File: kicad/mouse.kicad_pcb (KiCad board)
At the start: 2 copper layers, 77 parts, among them IC1 L7805, P1 SOURCE_12v, P10 LED_CONN, P11 SW_CONN, P12 LED_K_CONN, P13 IR_SOURCE, P14 IR_CONN, P15 UI_SOURCE, P16 LED_K_CONN, P17 LED_CONN, P18 SW_CONN, P19 in12v -+ MOTOR_SOURCE, P2 SOURCE_12v, P20 in5v -+ CHIP_SOURCE, P21 MOTOR_CONTROL MOTOR_CONTROL, P22 MOTOR_L, P23 MOTOR_R, P3 battery 12v, P4 SOURCE_5v, P5 SOURCE_5v, P6 SOURCE_5v, P7 SOURCE_5v, P8 IR_CONN, P9 MOTOR_CONTROL, Q1 BSS138, Q2 BSS138, Q3 BSS138, Q4 BSS138, Q5 BSS138, Q6 BSS138, Q7 BSS138, SW1 SPST, SW2 SW_PUSH, SW3 SW_PUSH, SW4 SW_PUSH, U1 MCP3008, U2 LBR-127HLD, U3 LBR-127HLD, U4 LBR-127HLD, U5 LBR-127HLD

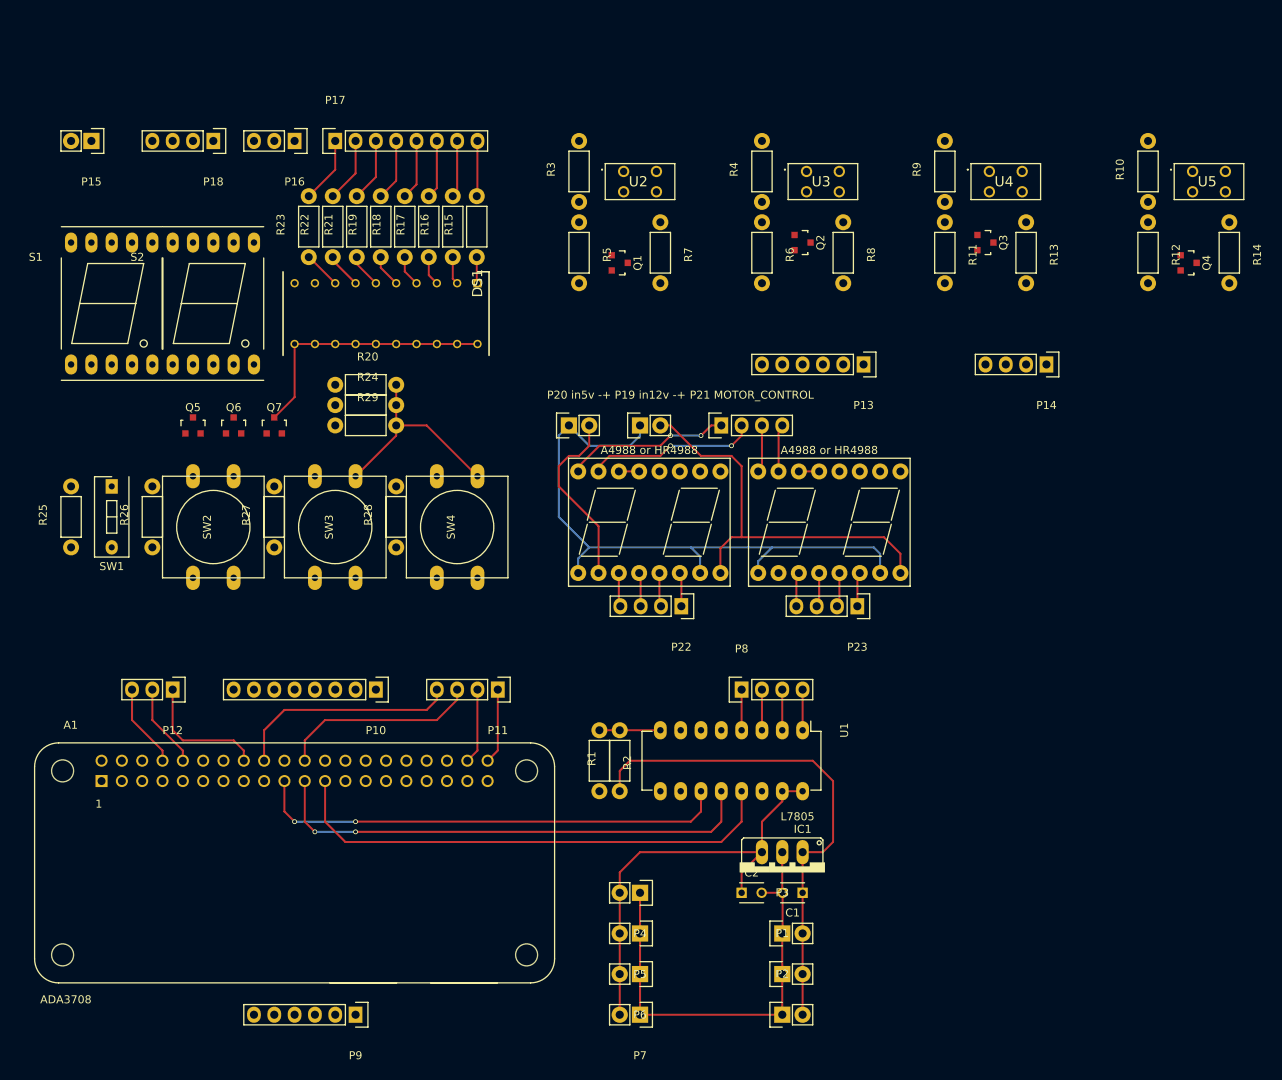
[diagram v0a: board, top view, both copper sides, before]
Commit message: add kicad
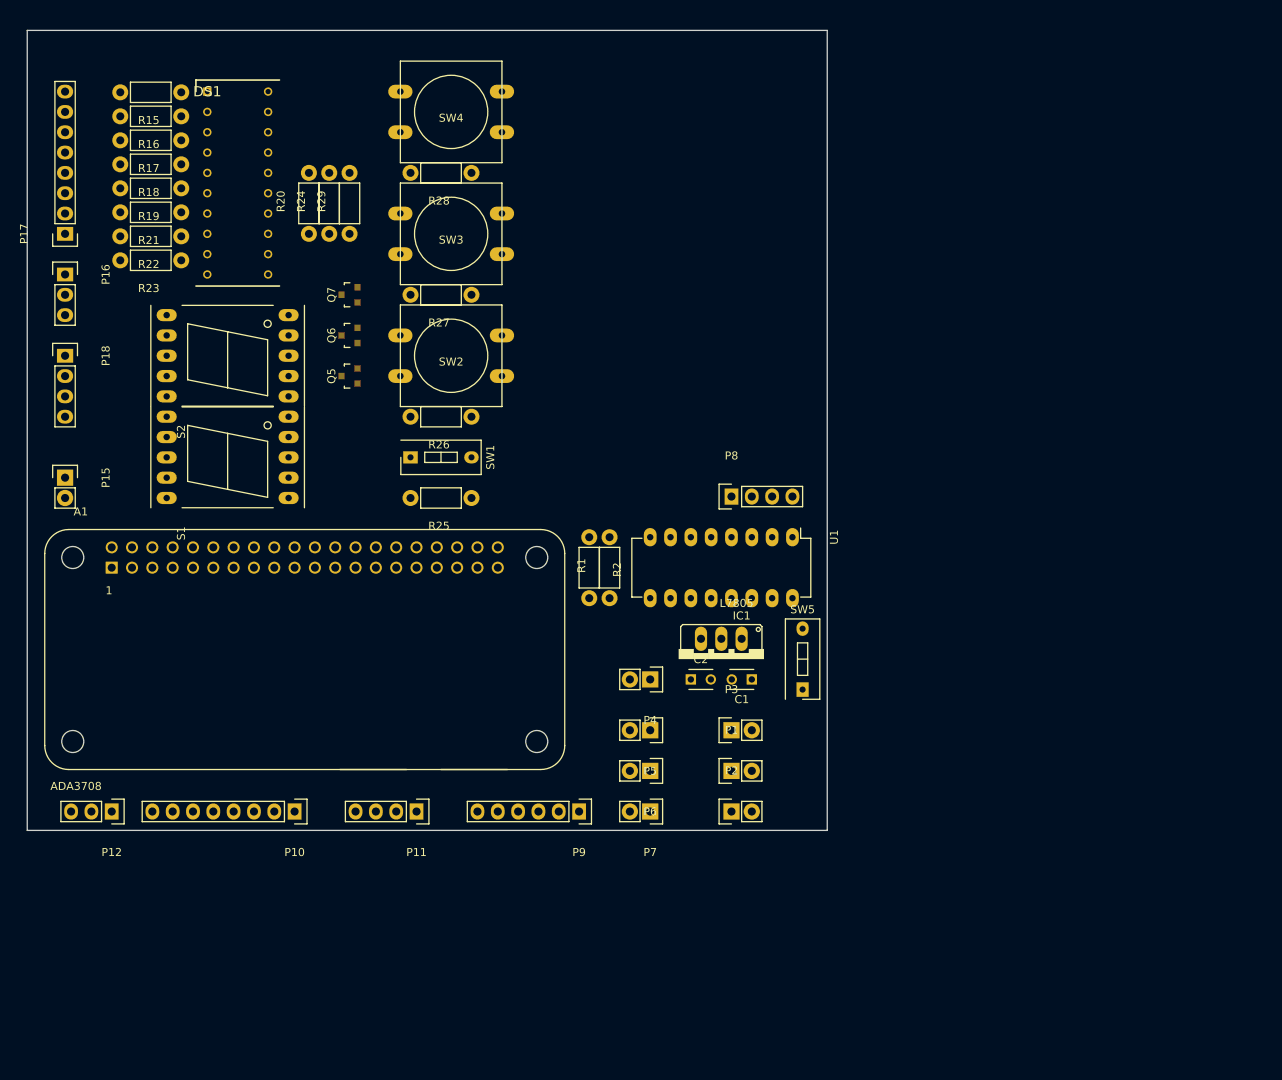
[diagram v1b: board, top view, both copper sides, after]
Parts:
- removed A4988 or HR4988: POLOLU_A4988, Displays_7-Segment:DA04 (x2)
- removed P13: IR_SOURCE, Socket_Strips:Socket_Strip_Straight_1x06
- removed P14: IR_CONN, Socket_Strips:Socket_Strip_Straight_1x04
- removed P19 in12v -+: MOTOR_SOURCE, Socket_Strips:Socket_Strip_Straight_1x02
- removed P20 in5v -+: CHIP_SOURCE, Socket_Strips:Socket_Strip_Straight_1x02
- removed P21 MOTOR_CONTROL: MOTOR_CONTROL, Socket_Strips:Socket_Strip_Straight_1x04
- removed P22: MOTOR_L, Socket_Strips:Socket_Strip_Straight_1x04
- removed P23: MOTOR_R, Socket_Strips:Socket_Strip_Straight_1x04
- removed Q1, Q2, Q3, Q4: BSS138, TO_SOT_Packages_SMD:SOT-23
- removed R10, R3, R4, R9: 10, Resistors_ThroughHole:Resistor_Horizontal_RM7mm
- removed R11, R12, R5, R6: 10k, Resistors_ThroughHole:Resistor_Horizontal_RM7mm
- removed R13, R14, R7, R8: 1k, Resistors_ThroughHole:Resistor_Horizontal_RM7mm
- removed U2, U3, U4, U5: LBR-127HLD, LBR-127HLD:A5131A
- added SW5: SPST, Buttons_Switches_ThroughHole:SW_DIP_x1_Slide, F.Cu at (121.9, 152.4)
- moved SW4 51.9 mm to (78.0, 80.2), turned to 180 degrees
- moved R25 50.4 mm to (80.5, 128.4), turned to 180 degrees
- moved R28 47.7 mm to (80.5, 87.8), turned to 180 degrees
- moved R26 43.1 mm to (80.5, 118.3), turned to 180 degrees
- moved R15 42.3 mm to (44.2, 77.7), turned to 180 degrees
- moved P15 42.2 mm to (29.7, 125.9), turned to 270 degrees
- moved DS1 41.4 mm to (47.5, 77.7), turned to 0 degrees
- moved R27 40.1 mm to (80.5, 103.0), turned to 180 degrees
- moved SW3 39.4 mm to (78.0, 95.4), turned to 180 degrees
- moved R16 38.2 mm to (44.2, 80.7), turned to 180 degrees
- moved P9 37.8 mm to (94.0, 167.6)
- moved SW1 37.5 mm to (72.9, 123.4), turned to 270 degrees
- moved SW2 36.6 mm to (78.0, 110.7), turned to 180 degrees
- moved P17 35.7 mm to (29.7, 95.4), turned to 90 degrees
- moved R17 34.2 mm to (44.2, 83.7), turned to 180 degrees
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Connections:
- P3 pad 2: Net-(C1-Pad1) -> Net-(P3-Pad2)
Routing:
- net Net-(P19-Pad1): track 79.6 -> 0.00 mm
- net Net-(C1-Pad1): track 63.1 -> 0.00 mm
- net Net-(A1-Pad23): track 63.1 -> 0.00 mm
- net Net-(A1-Pad21): track 62.0 -> 0.00 mm, vias 2 -> 0
- net Net-(A1-Pad19): track 59.5 -> 0.00 mm, vias 2 -> 0
- net GND: track 55.9 -> 0.00 mm
- net +5V: track 54.0 -> 0.00 mm
- net Net-(P19-Pad2): track 50.6 -> 0.00 mm
- net Net-(DS1-Pad11): track 33.1 -> 0.00 mm
- net SW1: track 28.2 -> 0.00 mm
- net Net-(P15-Pad1): track 26.3 -> 0.00 mm
- net SW2: track 25.0 -> 0.00 mm
- net Net-(P20-Pad2): track 22.8 -> 0.00 mm
- net Net-(P21-Pad2): track 21.9 -> 0.00 mm, vias 2 -> 0
- net Net-(P21-Pad1): track 21.2 -> 0.00 mm, vias 2 -> 0
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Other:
- board outline added: 100 x 100 mm

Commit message: add kicad
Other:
- board text added: "MechanicPlatypus MicroMouse"
- board text added: "made by powertimer811"
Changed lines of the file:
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@@
     (area 0 0 0 0)
     (thickness 1.6)
-    (drawings 6)
+    (drawings 8)
     (tracks 0)
     (zones 0)
@@
     )
   )
+  (gr_text "made by powertimer811" (at 120 90 90) (layer F.SilkS)
+    (effects (font (size 2 2) (thickness 0.3) italic))
+  )
+  (gr_text "MechanicPlatypus\nMicroMouse" (at 95 100 90) (layer F.SilkS)
+    (effects (font (size 4 4) (thickness 0.3) italic))
+  )
   (gr_line (start 125 70) (end 25 70) (angle 90) (layer Edge.Cuts) (width 0.15))

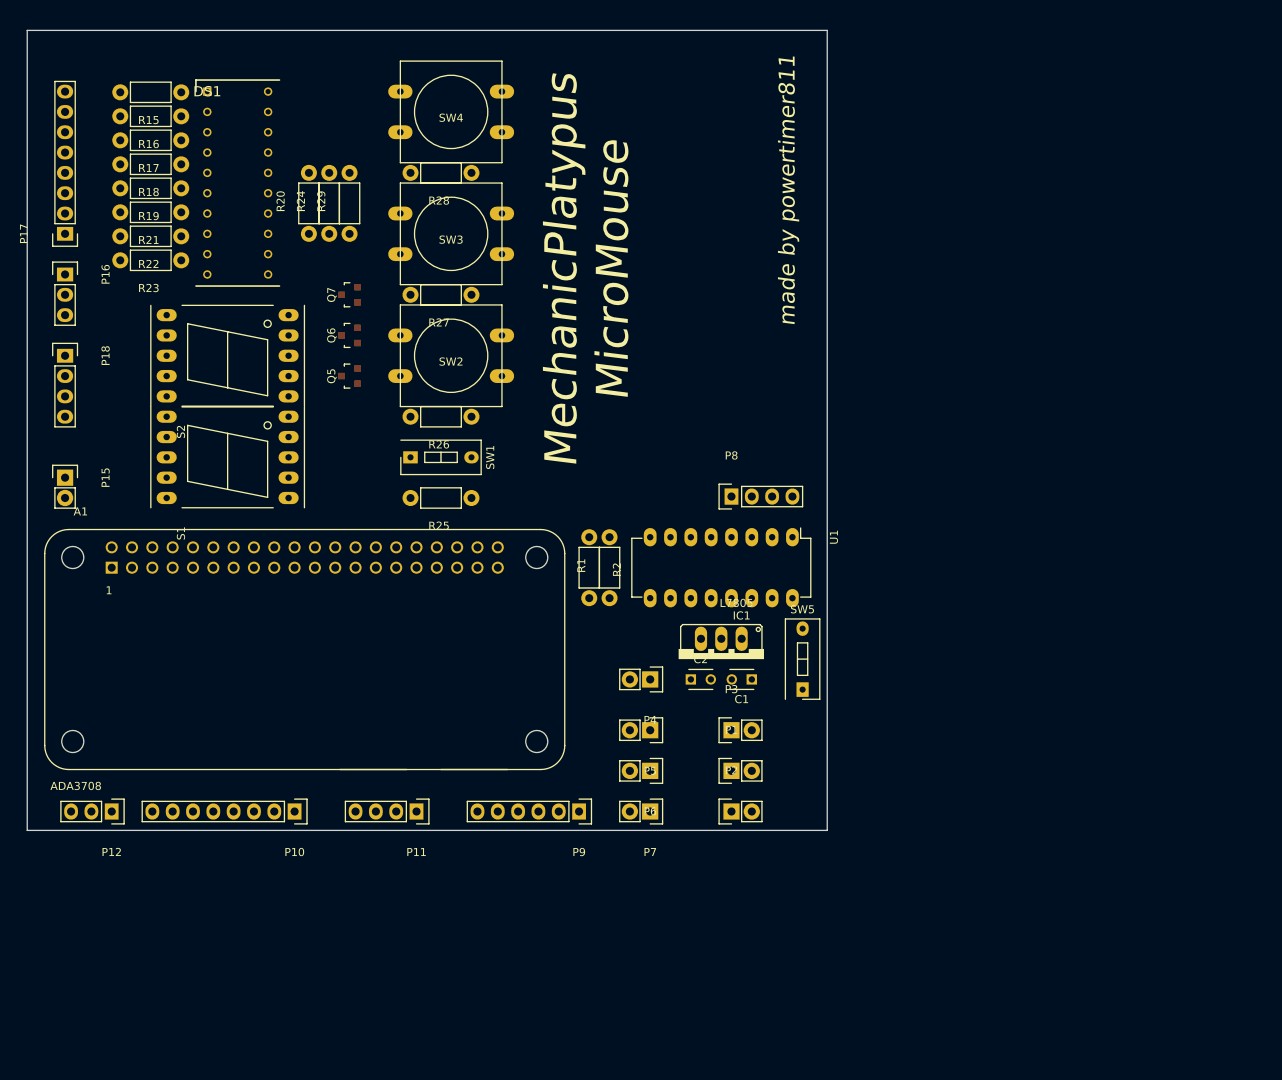
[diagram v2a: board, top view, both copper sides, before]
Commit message: rotate raspberry pi
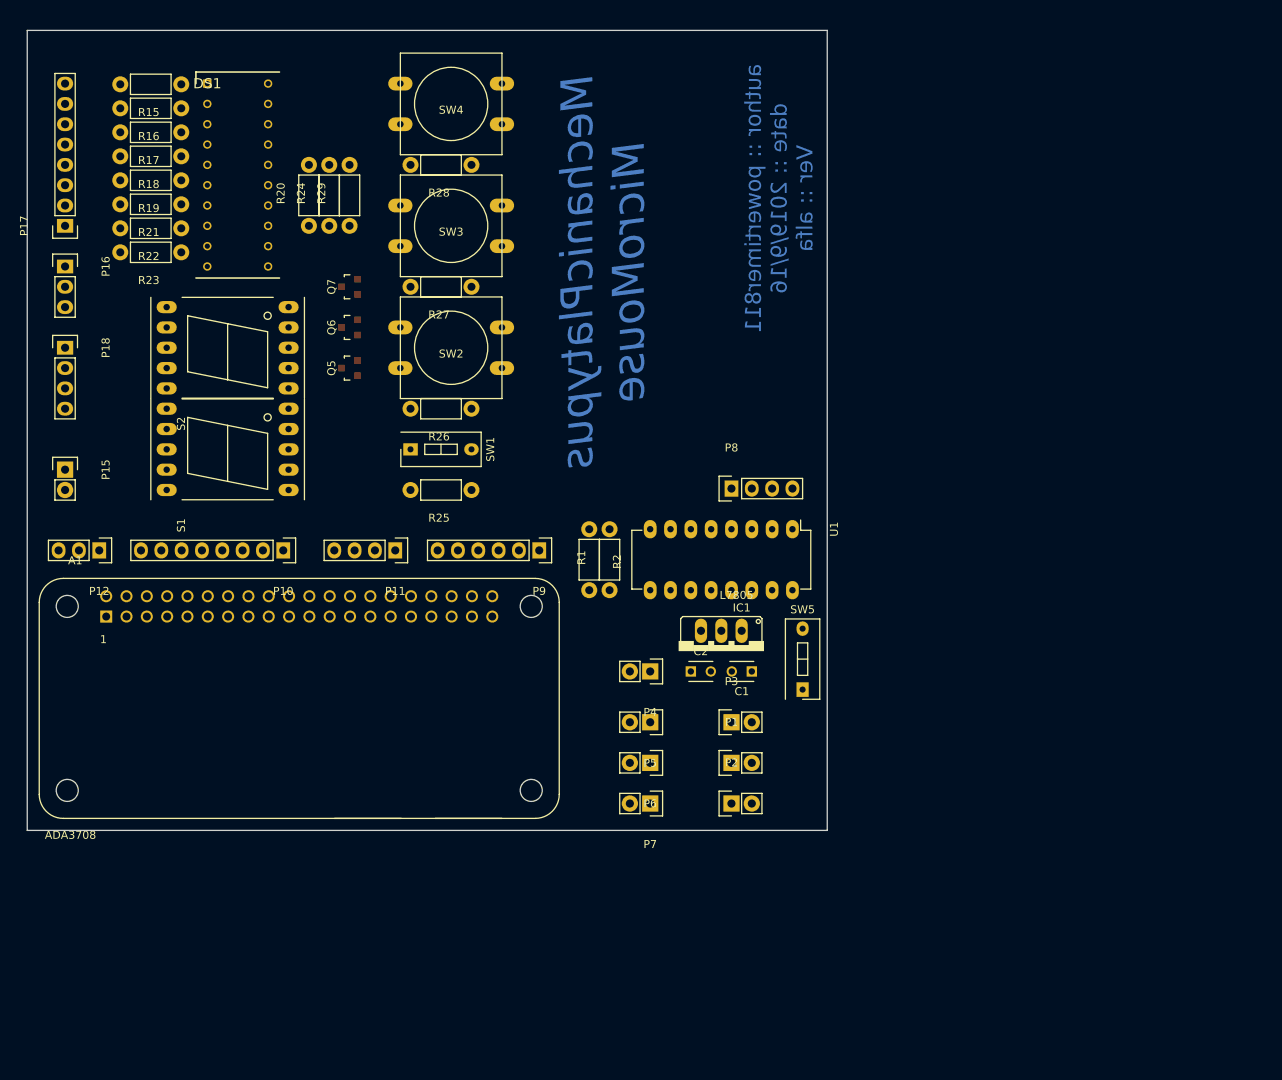
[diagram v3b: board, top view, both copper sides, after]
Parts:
- moved P9 33.0 mm to (89.0, 135.0)
- moved P11 32.7 mm to (71.0, 135.0)
- moved P12 32.7 mm to (34.0, 135.0)
- moved P10 32.7 mm to (57.0, 135.0)
- moved A1 6.15 mm to (59.0, 142.0)
- moved P8 1.00 mm to (113.0, 127.3)
- moved C1 1.00 mm to (115.6, 150.1)
- moved C2 1.00 mm to (108.0, 150.1)
- moved DS1 1.00 mm to (47.5, 76.7)
- moved IC1 1.00 mm to (111.8, 147.6)
- moved P1 1.00 mm to (113.0, 161.6)
- moved P15 1.00 mm to (29.7, 124.9)
- moved P16 1.00 mm to (29.7, 99.5)
- moved P17 1.00 mm to (29.7, 94.4)
- moved P18 1.00 mm to (29.7, 109.7)
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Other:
- board text added: "author :: powertimer811 date :: 2019/9/16 Ver :: alfa"
- board text removed: "made by powertimer811"

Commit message: complate kicad
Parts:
- moved P9 66.7 mm to (30.1, 166.3), turned to 0 degrees
- moved P12 59.9 mm to (85.1, 166.3), turned to 0 degrees
- moved P11 38.8 mm to (48.1, 166.3), turned to 0 degrees
- moved P10 31.7 mm to (62.1, 166.3), turned to 0 degrees
- moved A1 17.3 mm to (60.1, 159.3), turned to 180 degrees
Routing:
- net Net-(P15-Pad1): track 0.00 -> 166.7 mm
- net GND: track 0.00 -> 155.4 mm
- net Net-(P16-Pad1): track 0.00 -> 141.6 mm
- net Net-(P15-Pad2): track 0.00 -> 93.4 mm
- net Net-(P18-Pad1): track 0.00 -> 90.8 mm
- net Net-(P18-Pad2): track 0.00 -> 88.3 mm
- net Net-(P18-Pad3): track 0.00 -> 74.4 mm
- net Net-(P16-Pad2): track 0.00 -> 72.1 mm
- net Net-(P16-Pad3): track 0.00 -> 69.1 mm
- net Net-(A1-Pad23): track 0.00 -> 65.8 mm
- net +5V: track 0.00 -> 63.4 mm
- net Net-(A1-Pad21): track 0.00 -> 60.7 mm
- net Net-(A1-Pad24): track 0.00 -> 58.9 mm
- net Net-(DS1-Pad4): track 0.00 -> 55.3 mm
- net Net-(P18-Pad4): track 0.00 -> 54.4 mm
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- added copper zone on B.Cu, net GND
- added copper zone on F.Cu, net GND
